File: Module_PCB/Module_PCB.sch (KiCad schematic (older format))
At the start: 109 parts, among them J2 ISP, J4 DS, J5 US, Q1 KIA50N03B, Q2 KIA50N03B, Q3 KIA50N03B, Q4 KIA50N03B, U1 W25Q16JV, U2 AP1117-33, U3 TPS563200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

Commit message: Changed name from LEDStripModule to Module_PCB of the Kicad project
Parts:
- U1: symbol LEDStripModule:W25Q16JV -> Module_PCB:W25Q16JV
- U4, U6: symbol LEDStripModule:AP9101CK6 -> Module_PCB:AP9101CK6
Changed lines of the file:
@@
 $EndComp
 $Comp
-L LEDStripModule:W25Q16JV U1
+L Module_PCB:W25Q16JV U1
 U 1 1 60D73EDF
 P 1100 6550
@@
 Connection ~ 1200 2000
 $Comp
-L LEDStripModule:AP9101CK6 U4
+L Module_PCB:AP9101CK6 U4
 U 1 1 60D8F4A2
 P 1950 1250
@@
 	4100 900  4100 850
 $Comp
-L LEDStripModule:AP9101CK6 U6
+L Module_PCB:AP9101CK6 U6
 U 1 1 60DA476D
 P 4100 1200

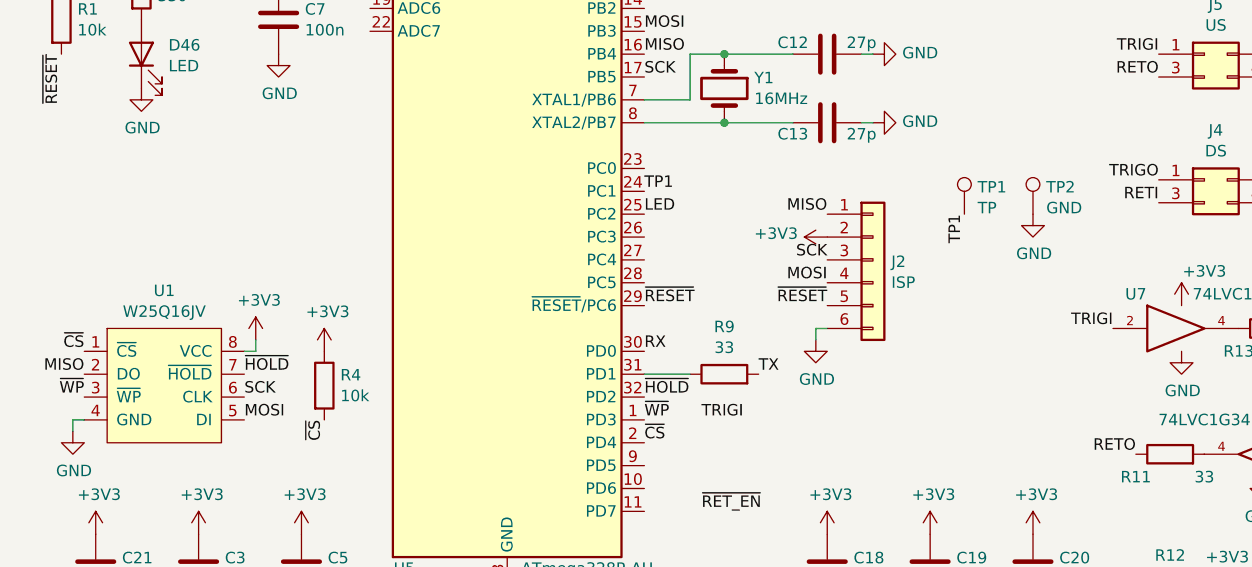
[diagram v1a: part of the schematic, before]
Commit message: Changed ISP header back to 2x3
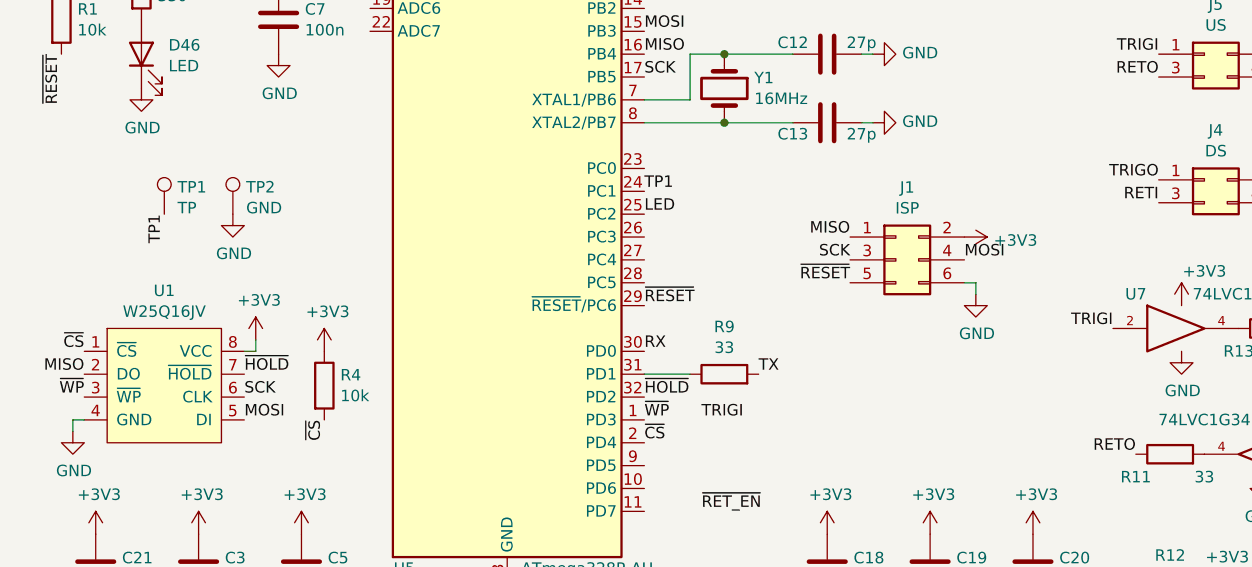
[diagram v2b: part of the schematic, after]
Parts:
- removed J2: ISP, Connector_PinHeader_2.54mm:PinHeader_1x06_P2.54mm_Vertical, symbol Connector_Generic:Conn_01x06
- added J1: ISP, Connector_PinHeader_2.54mm:PinHeader_2x03_P2.54mm_Vertical, symbol Connector_Generic:Conn_02x03_Odd_Even
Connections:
- net +3V3: now also J1.2 (Pin_2)
- net GND: now also J1.6 (Pin_6)
- net MISO: now also J1.1 (Pin_1)
- net MOSI: now also J1.4 (Pin_4)
- net SCK: now also J1.3 (Pin_3)
- net ~RESET: now also J1.5 (Pin_5)
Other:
- moved on the sheet: TP1, TP2
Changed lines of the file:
@@
 Text Label 5450 5200 2    50   ~ 0
 RETO
-$Comp
-L Connector_Generic:Conn_01x06 J2
-U 1 1 614FDEE4
-P 4200 6000
-F 0 "J2" H 4280 5992 50  0000 L CNN
-F 1 "ISP" H 4280 5901 50  0000 L CNN
-F 2 "Connector_PinHeader_2.54mm:PinHeader_1x06_P2.54mm_Vertical" H 4200 6000 50  0001 C CNN
-F 3 "~" H 4200 6000 50  0001 C CNN
-F 4 "MINTRON" H 4200 6000 50  0001 C CNN "Manufacturer"
-F 5 "MTP125-1106S1" H 4200 6000 50  0001 C CNN "MPN"
-	1    4200 6000
-	1    0    0    -1
-$EndComp
-Text Label 4000 5800 2    50   ~ 0
+Text Label 4100 5900 2    50   ~ 0
 MISO
 $Comp
 L power:+3V3 #PWR0141
 U 1 1 614FE44E
-P 4000 5900
-F 0 "#PWR0141" H 4000 5750 50  0001 C CNN
-F 1 "+3V3" V 4015 6028 50  0000 L CNN
-F 2 "" H 4000 5900 50  0001 C CNN
-F 3 "" H 4000 5900 50  0001 C CNN
-	1    4000 5900
-	0    -1   -1   0
-$EndComp
-Text Label 4000 6000 2    50   ~ 0
+P 4600 5900
+F 0 "#PWR0141" H 4600 5750 50  0001 C CNN
+F 1 "+3V3" V 4615 6028 50  0000 L CNN
+F 2 "" H 4600 5900 50  0001 C CNN
+F 3 "" H 4600 5900 50  0001 C CNN
+	1    4600 5900
+	0    1    1    0
+$EndComp
+Text Label 4100 6000 2    50   ~ 0
 SCK
-Text Label 4000 6100 2    50   ~ 0
+Text Label 4600 6000 0    50   ~ 0
 MOSI
-Text Label 4000 6200 2    50   ~ 0
+Text Label 4100 6100 2    50   ~ 0
 ~RESET
 $Comp
 L power:GND #PWR0142
 U 1 1 614FEE87
-P 3950 6350
-F 0 "#PWR0142" H 3950 6100 50  0001 C CNN
-F 1 "GND" H 3955 6177 50  0000 C CNN
-F 2 "" H 3950 6350 50  0001 C CNN
-F 3 "" H 3950 6350 50  0001 C CNN
-	1    3950 6350
-	1    0    0    -1
-$EndComp
-Wire Wire Line
-	4000 6300 3950 6300
-Wire Wire Line
-	3950 6300 3950 6350
+P 4650 6150
+F 0 "#PWR0142" H 4650 5900 50  0001 C CNN
+F 1 "GND" H 4655 5977 50  0000 C CNN
+F 2 "" H 4650 6150 50  0001 C CNN
+F 3 "" H 4650 6150 50  0001 C CNN
+	1    4650 6150
+	1    0    0    -1
+$EndComp
 Text Label 5950 5100 0    50   ~ 0
 RX
@@
 L Connector:TestPoint TP1
 U 1 1 60DA3249
-P 4600 5800
-F 0 "TP1" H 4658 5918 50  0000 L CNN
-F 1 "TP" H 4658 5827 50  0000 L CNN
-F 2 "TestPoint:TestPoint_Pad_D1.5mm" H 4800 5800 50  0001 C CNN
-F 3 "~" H 4800 5800 50  0001 C CNN
-	1    4600 5800
+P 1100 5800
+F 0 "TP1" H 1158 5918 50  0000 L CNN
+F 1 "TP" H 1158 5827 50  0000 L CNN
+F 2 "TestPoint:TestPoint_Pad_D1.5mm" H 1300 5800 50  0001 C CNN
+F 3 "~" H 1300 5800 50  0001 C CNN
+	1    1100 5800
 	1    0    0    -1
 $EndComp
@@
 L Connector:TestPoint TP2
 U 1 1 60DA37C3
-P 4900 5800
-F 0 "TP2" H 4958 5918 50  0000 L CNN
-F 1 "GND" H 4958 5827 50  0000 L CNN
-F 2 "TestPoint:TestPoint_Pad_D1.5mm" H 5100 5800 50  0001 C CNN
-F 3 "~" H 5100 5800 50  0001 C CNN
-	1    4900 5800
+P 1400 5800
+F 0 "TP2" H 1458 5918 50  0000 L CNN
+F 1 "GND" H 1458 5827 50  0000 L CNN
+F 2 "TestPoint:TestPoint_Pad_D1.5mm" H 1600 5800 50  0001 C CNN
+F 3 "~" H 1600 5800 50  0001 C CNN
+	1    1400 5800
 	1    0    0    -1
 $EndComp
@@
 L power:GND #PWR0147
 U 1 1 60DA3BA0
-P 4900 5800
-F 0 "#PWR0147" H 4900 5550 50  0001 C CNN
-F 1 "GND" H 4905 5627 50  0000 C CNN
-F 2 "" H 4900 5800 50  0001 C CNN
-F 3 "" H 4900 5800 50  0001 C CNN
-	1    4900 5800
-	1    0    0    -1
-$EndComp
-Text Label 4600 5800 3    50   ~ 0
+P 1400 5800
+F 0 "#PWR0147" H 1400 5550 50  0001 C CNN
+F 1 "GND" H 1405 5627 50  0000 C CNN
+F 2 "" H 1400 5800 50  0001 C CNN
+F 3 "" H 1400 5800 50  0001 C CNN
+	1    1400 5800
+	1    0    0    -1
+$EndComp
+Text Label 1100 5800 3    50   ~ 0
 TP1
 Text Label 3200 5700 0    50   ~ 0
 TP1
+$Comp
+L Connector_Generic:Conn_02x03_Odd_Even J1
+U 1 1 60D97074
+P 4300 6000
+F 0 "J1" H 4350 6317 50  0000 C CNN
+F 1 "ISP" H 4350 6226 50  0000 C CNN
+F 2 "Connector_PinHeader_2.54mm:PinHeader_2x03_P2.54mm_Vertical" H 4300 6000 50  0001 C CNN
+F 3 "~" H 4300 6000 50  0001 C CNN
+F 4 "PINREX" H 4300 6000 50  0001 C CNN "Manufacturer"
+F 5 "210-72-03GB01" H 4300 6000 50  0001 C CNN "MPN"
+	1    4300 6000
+	1    0    0    -1
+$EndComp
+Wire Wire Line
+	4600 6100 4650 6100
+Wire Wire Line
+	4650 6100 4650 6150
 $EndSCHEMATC

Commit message: Fixed MPN
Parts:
- U8: MPN 74LVC1G34 -> 74LVC1G34GW,125
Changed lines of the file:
@@
 F 3 "http://www.ti.com/lit/sg/scyt129e/scyt129e.pdf" H 5900 6850 50  0001 C CNN
 F 4 "Nexperia" H 5900 6850 50  0001 C CNN "Manufacturer"
-F 5 "74LVC1G34" H 5900 6850 50  0001 C CNN "MPN"
+F 5 "74LVC1G34GW,125" H 5900 6850 50  0001 C CNN "MPN"
 	1    5900 6850
 	-1   0    0    -1

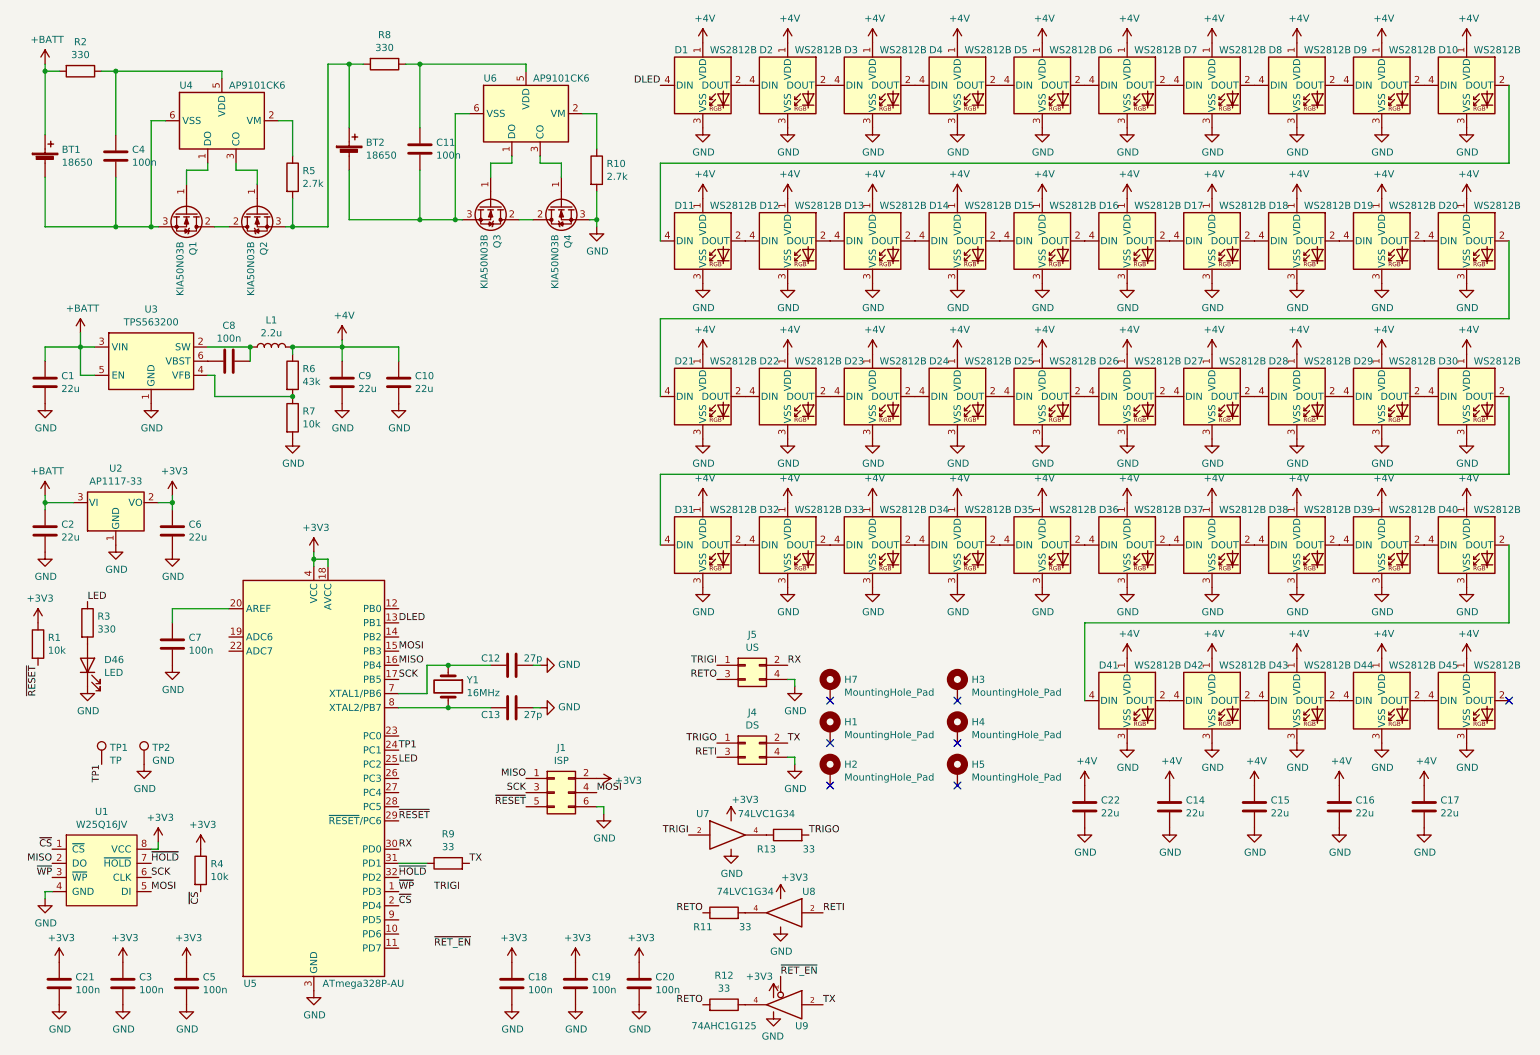
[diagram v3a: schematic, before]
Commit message: Changed the battery protection method and added a turn-on wire for the master
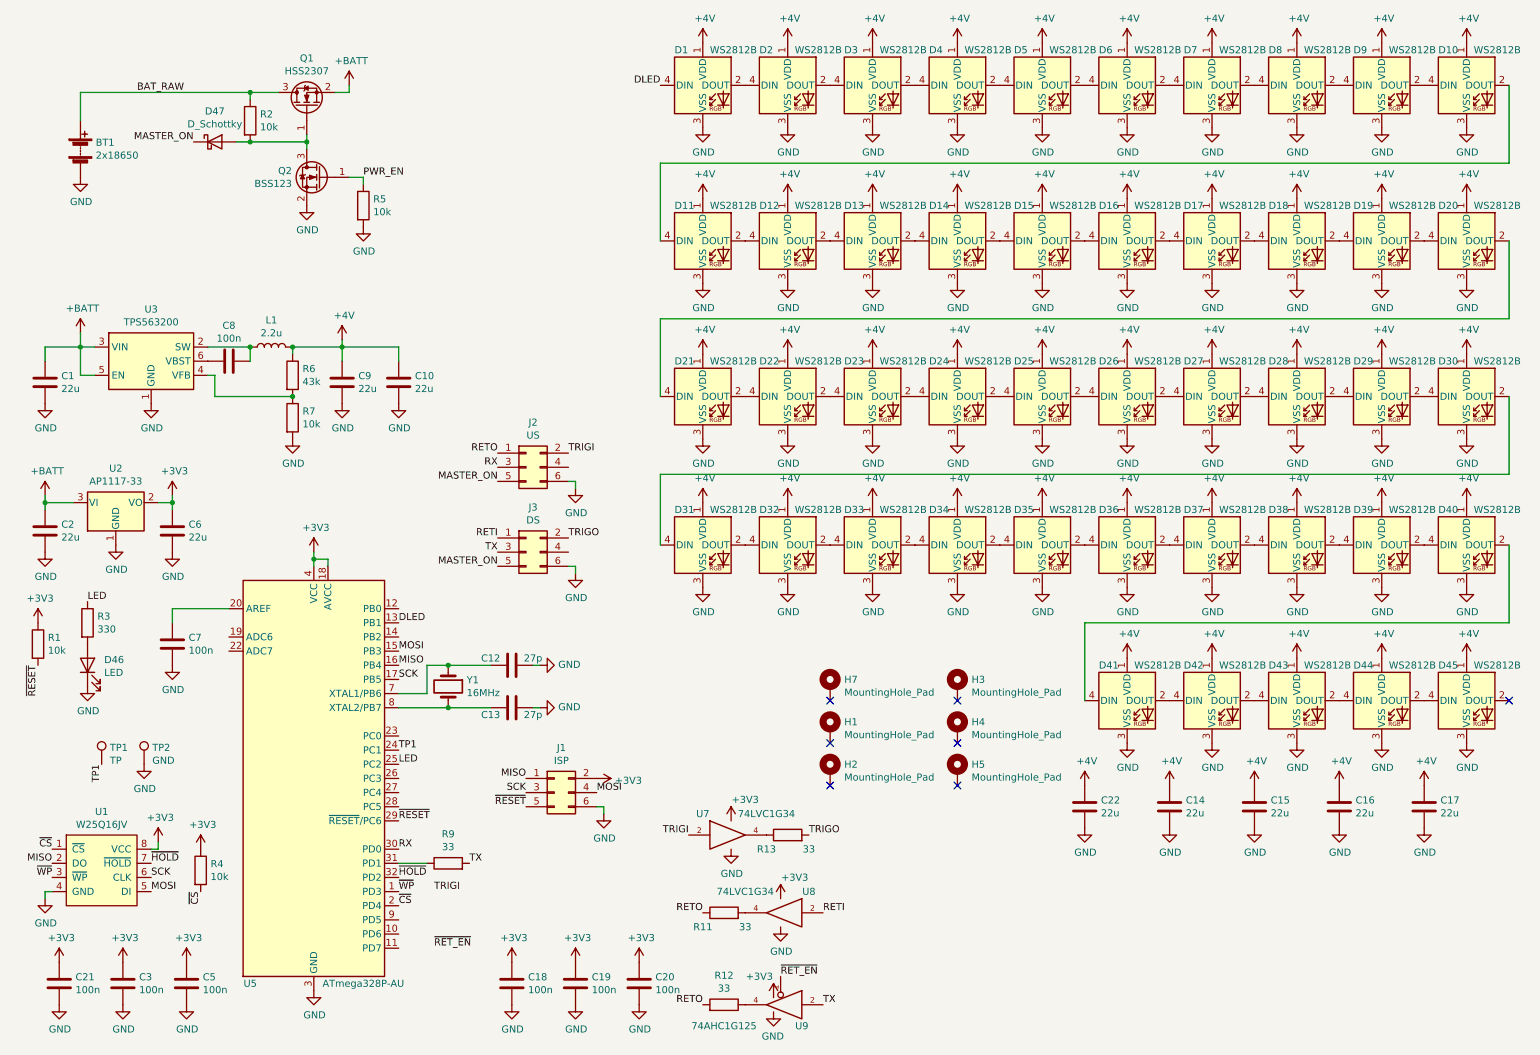
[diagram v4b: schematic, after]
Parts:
- removed BT1, BT2: 18650, Connector_PinHeader_2.54mm:PinHeader_1x02_P2.54mm_Vertical, symbol Device:Battery_Cell
- removed C11, C4: 100n, Capacitor_SMD:C_0603_1608Metric, symbol Device:C
- removed J4: DS, Connector_PinSocket_2.54mm:PinSocket_2x02_P2.54mm_Horizontal, symbol Connector_Generic:Conn_02x02_Odd_Even
- removed J5: US, Connector_PinHeader_2.54mm:PinHeader_2x02_P2.54mm_Horizontal, symbol Connector_Generic:Conn_02x02_Odd_Even
- removed Q1, Q2, Q3, Q4: KIA50N03B, Package_TO_SOT_SMD:TO-252-2, symbol Device:Q_NMOS_GDS
- removed R10: 2.7k, Resistor_SMD:R_0603_1608Metric, symbol Device:R
- removed R8: 330, Resistor_SMD:R_0603_1608Metric, symbol Device:R
- removed U4, U6: AP9101CK6, Package_TO_SOT_SMD:SOT-23-6, symbol Module_PCB:AP9101CK6
- added BT1: 2x18650, Connector_PinHeader_2.54mm:PinHeader_2x01_P2.54mm_Vertical, symbol Device:Battery
- added D47: D_Schottky, Diode_SMD:D_SOD-123, symbol Device:D_Schottky
- added J2: US, Connector_PinHeader_2.54mm:PinHeader_2x03_P2.54mm_Horizontal, symbol Connector_Generic:Conn_02x03_Odd_Even
- added J3: DS, Connector_PinSocket_2.54mm:PinSocket_2x03_P2.54mm_Horizontal, symbol Connector_Generic:Conn_02x03_Odd_Even
- added Q1: HSS2307, Package_TO_SOT_SMD:SOT-23, symbol Device:Q_NMOS_GSD
- added Q2: BSS123, Package_TO_SOT_SMD:SOT-23, symbol Transistor_FET:BSS123
- R2: value 330 -> 10k; MPN RC0603FR-07330RL -> RC0603JR-0710KL
- R5: value 2.7k -> 10k; MPN RC0603JR-072K7L -> RC0603JR-0710KL
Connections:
- net +BATT: now also Q1.2 (S); no longer R2.2
- net GND: now also R5.2, BT1.2 (-), J2.6 (Pin_6), J3.6 (Pin_6), Q2.2 (S)
- net RETI: now also J3.1 (Pin_1)
- net RETO: now also J2.1 (Pin_1)
- net RX: now also J2.3 (Pin_3)
- net TRIGI: now also J2.2 (Pin_2)
- net TRIGO: now also J3.2 (Pin_2)
- net TX: now also J3.3 (Pin_3)
- net BAT_RAW: now reaches R2.1
- net BAT_RAW: now also BT1.1 (+), Q1.3 (D)
- net PWR_EN: now reaches R5.1
- net PWR_EN: now also Q2.1 (G)
- new net: D47.2 (A), Q1.1 (G), Q2.3 (D), R2.2
- new net MASTER_ON: D47.1 (K), J2.5 (Pin_5), J3.5 (Pin_5)

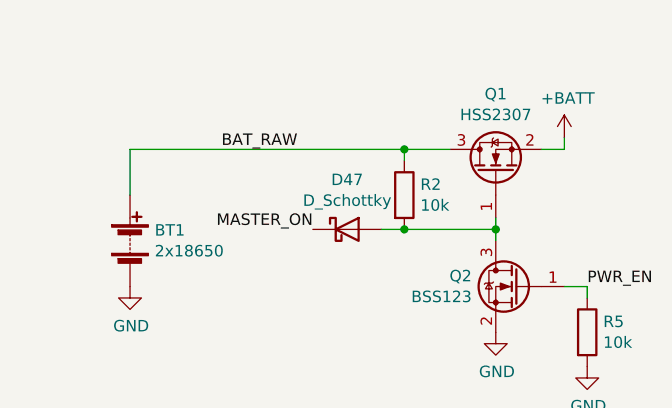
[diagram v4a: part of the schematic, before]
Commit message: Added a polyfuse, fixes #4
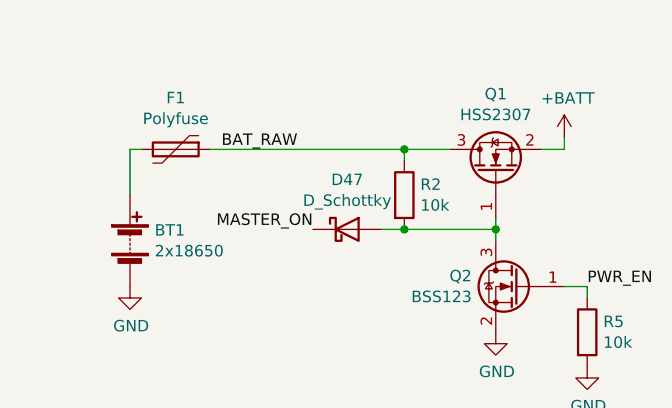
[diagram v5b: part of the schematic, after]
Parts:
- added F1: Polyfuse, Fuse:Fuse_1812_4532Metric_Castellated, symbol Device:Polyfuse
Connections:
- net BAT_RAW: now also F1.1; no longer BT1.1 (+)
- new net: BT1.1 (+), F1.2
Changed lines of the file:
@@
 $EndComp
 Wire Wire Line
-	950  1050 2150 1050
+	950  1050 1000 1050
 $Comp
 L Device:Battery BT1
@@
 Text Label 1350 1050 0    50   ~ 0
 BAT_RAW
+$Comp
+L Device:Polyfuse F1
+U 1 1 60DB9790
+P 1150 1050
+F 0 "F1" V 925 1050 50  0000 C CNN
+F 1 "Polyfuse" V 1016 1050 50  0000 C CNN
+F 2 "Fuse:Fuse_1812_4532Metric_Castellated" H 1200 850 50  0001 L CNN
+F 3 "~" H 1150 1050 50  0001 C CNN
+F 4 "BHFUSE " H 1150 1050 50  0001 C CNN "Manufacturer"
+F 5 "BSMD1812-200-30V" H 1150 1050 50  0001 C CNN "MPN"
+	1    1150 1050
+	0    1    1    0
+$EndComp
+Wire Wire Line
+	1300 1050 2150 1050
 $EndSCHEMATC
